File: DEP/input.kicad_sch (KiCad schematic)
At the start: 23 parts, among them U1 OPA2134, U2 PCM4201PWR

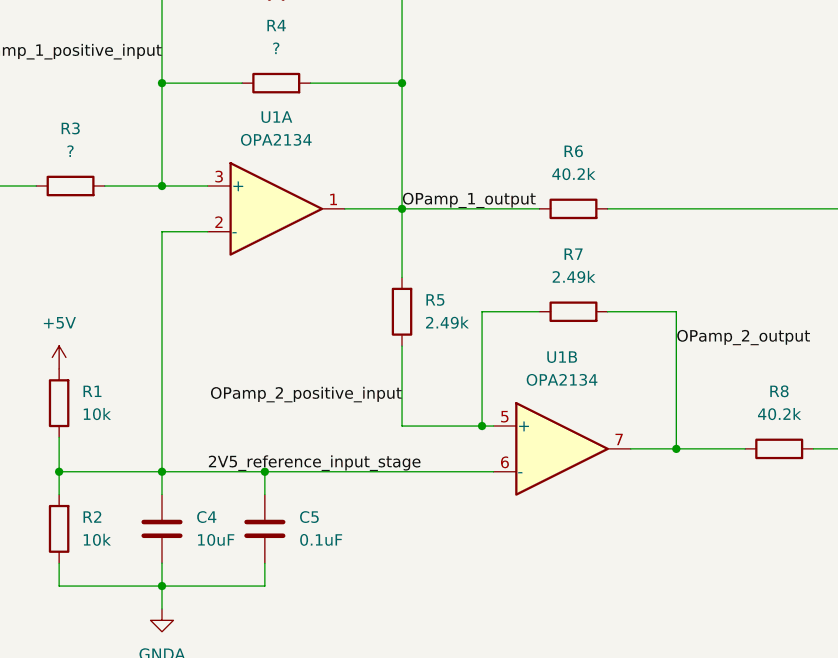
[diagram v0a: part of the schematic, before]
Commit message: fix +/- op-amp error...
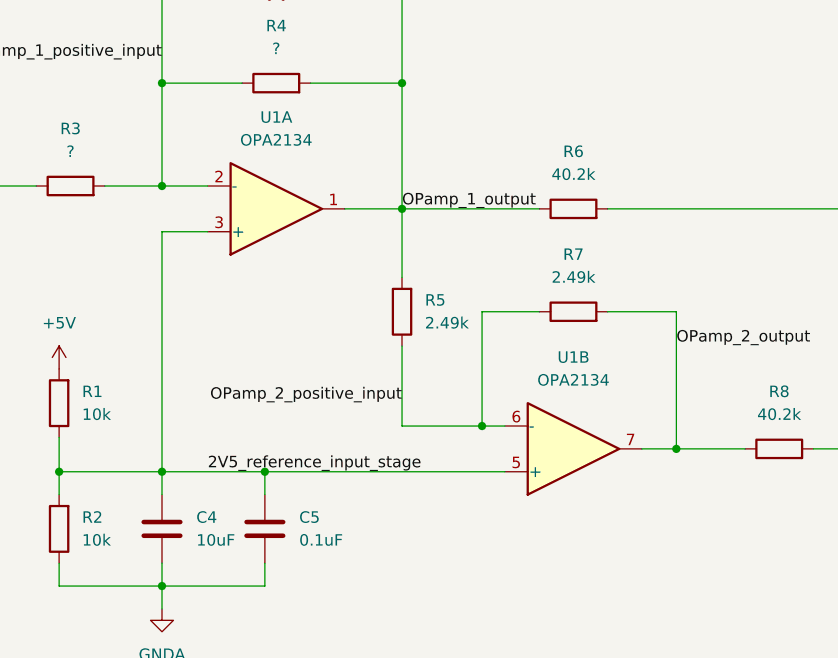
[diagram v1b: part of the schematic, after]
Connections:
- net 2V5_reference_input_stage: now also U1.3 (+), U1.5 (+); no longer U1.2 (-), U1.6 (-)
- net OPamp_1_positive_input: now also U1.2 (-); no longer U1.3 (+)
- net OPamp_2_positive_input: now also U1.6 (-); no longer U1.5 (+)
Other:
- moved on the sheet: U1B
